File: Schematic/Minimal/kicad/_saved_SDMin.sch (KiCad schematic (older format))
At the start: 6 parts

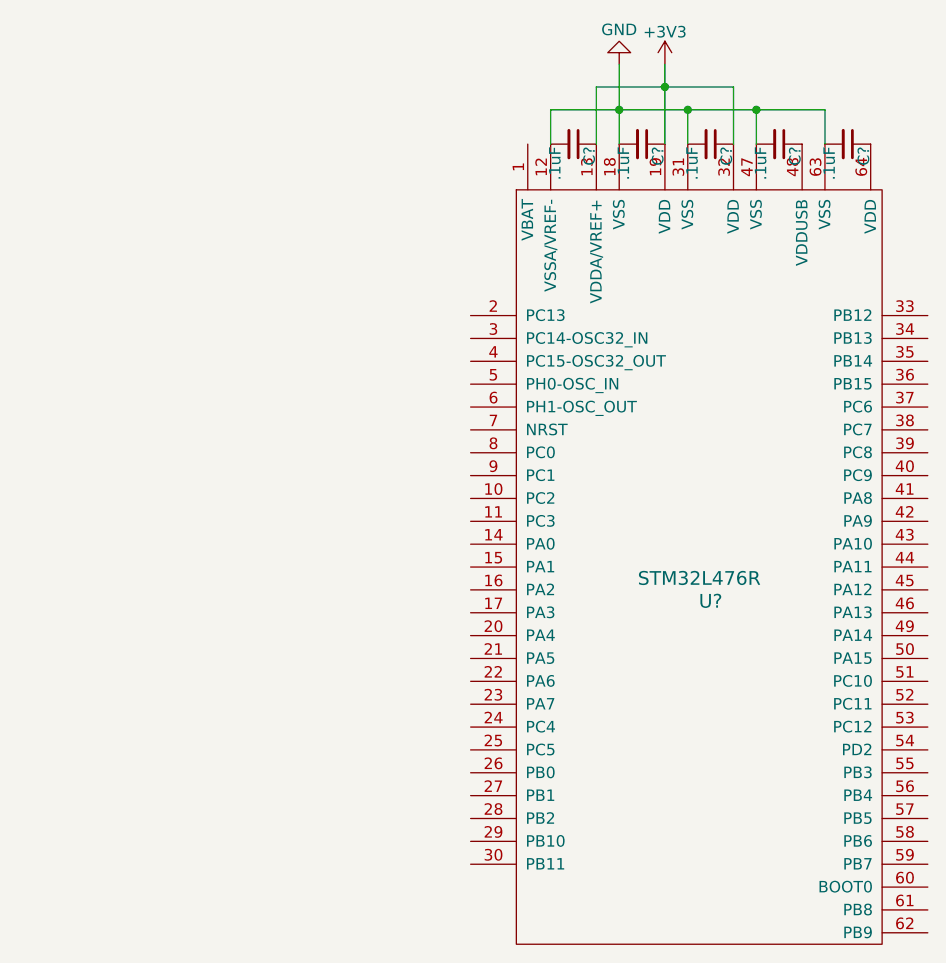
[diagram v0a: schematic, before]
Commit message: Work on minimal schematic, add power components
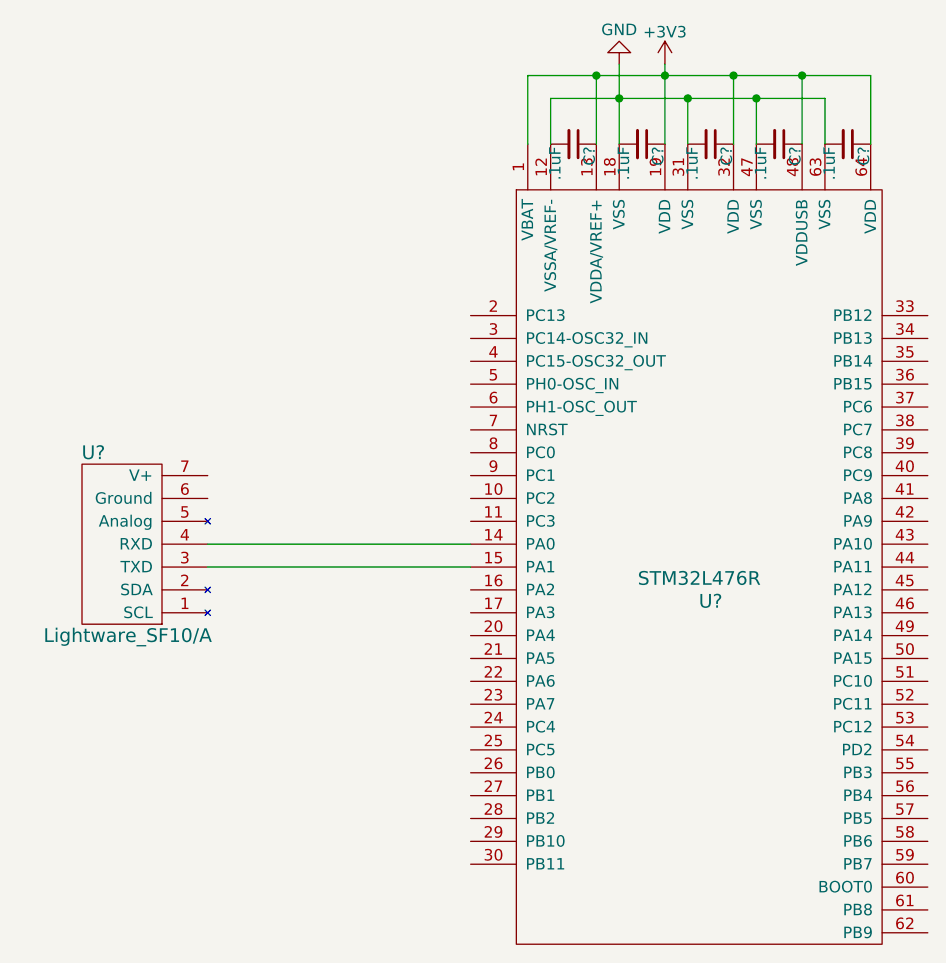
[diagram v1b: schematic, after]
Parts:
- added U?: Lightware_SF10/A, symbol Lightware_SF10/A
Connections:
- net +3V3: now also C?.1, C?.1, U?.1 (VBAT), U?.48 (VDDUSB), U?.64 (VDD)
- net at U?.14 (PA0): now also U?.4 (RXD)
- net at U?.15 (PA1): now also U?.3 (TXD)
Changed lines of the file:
@@
 	4750 1900 4750 1550
 Wire Wire Line
-	4850 1900 4850 1750
+	4850 1900 4850 1700
 Wire Wire Line
-	4250 1750 5450 1750
-Connection ~ 4550 1750
+	4250 1700 5450 1700
+Connection ~ 4550 1700
 Wire Wire Line
-	5150 1750 5150 1900
-Connection ~ 4850 1750
+	5150 1700 5150 1900
+Connection ~ 4850 1700
 Wire Wire Line
-	5450 1750 5450 1900
-Connection ~ 5150 1750
+	5450 1700 5450 1900
+Connection ~ 5150 1700
 Wire Wire Line
-	4250 1900 4250 1750
+	4250 1900 4250 1700
 Wire Wire Line
-	4450 1900 4450 1650
+	4150 1900 4150 1600
 Wire Wire Line
-	4450 1650 5050 1650
-Connection ~ 4750 1650
+	4150 1600 5650 1600
+Connection ~ 4750 1600
 Wire Wire Line
-	5050 1650 5050 1900
+	4450 1900 4450 1600
+Connection ~ 4450 1600
+Wire Wire Line
+	5050 1600 5050 1900
+Wire Wire Line
+	5350 1600 5350 1900
+Connection ~ 5050 1600
+Wire Wire Line
+	5650 1600 5650 1900
+Connection ~ 5350 1600
+$Comp
+L Lightware_SF10/A U?
+U 1 1 56B8F17D
+P 2450 3650
+F 0 "U?" H 2650 3250 60  0000 C CNN
+F 1 "Lightware_SF10/A" H 2500 4050 60  0000 C CNN
+F 2 "" H 2450 3650 60  0000 C CNN
+F 3 "" H 2450 3650 60  0000 C CNN
+	1    2450 3650
+	-1   0    0    1
+$EndComp
+Wire Wire Line
+	3900 3650 2750 3650
+Wire Wire Line
+	3900 3750 2750 3750
 $EndSCHEMATC
